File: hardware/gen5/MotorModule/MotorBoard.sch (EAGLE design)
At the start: 44 parts

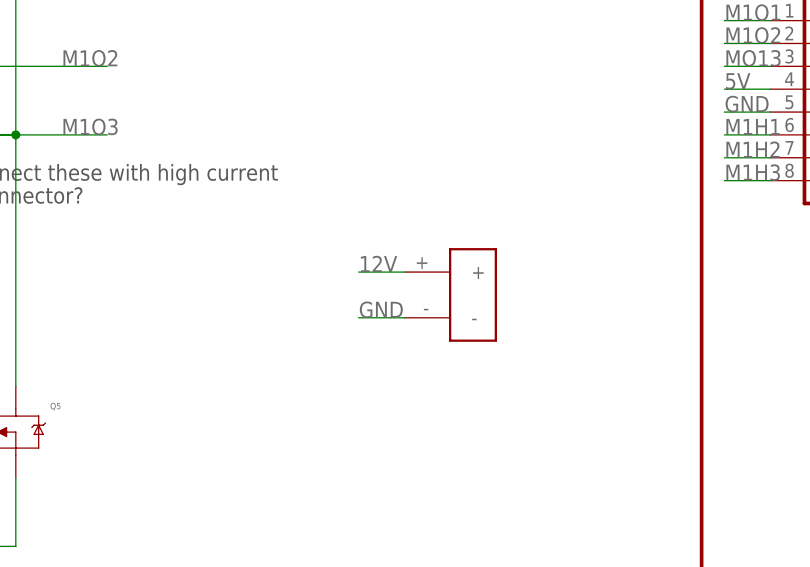
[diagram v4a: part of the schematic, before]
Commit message: placement ok - started rrouting
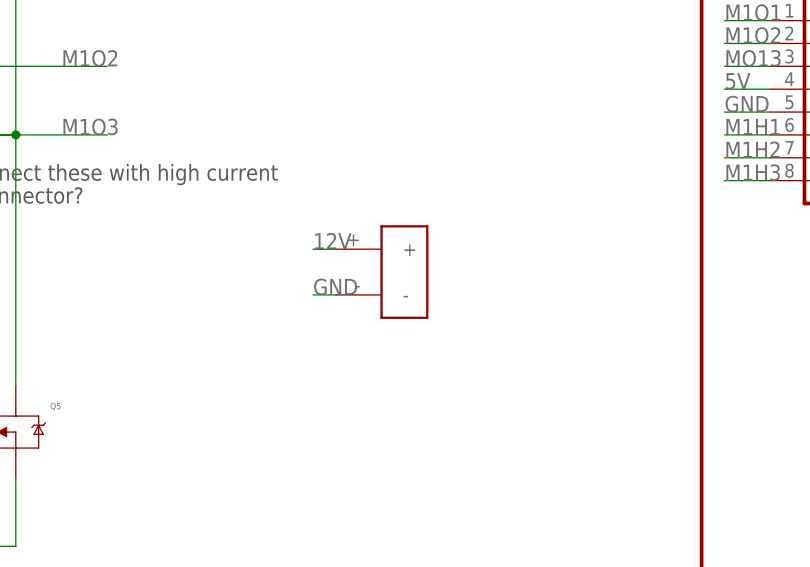
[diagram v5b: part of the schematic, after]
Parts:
- removed U$3: POWER_CONN_2X1, Kicker:POWER_CONN_2X1
- added U$2: POWER_CONN_2X1, Kicker:POWER_CONN_2X1
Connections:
- net 12V: now also U$2.+; no longer U$3.+
- net GND: now also U$2.-; no longer U$3.-
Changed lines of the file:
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@@
 <part name="J2" library="SparkFun-Connectors" library_urn="urn:adsk.eagle:library:513" deviceset="CONN_05X2" device="SHD" package3d_urn="urn:adsk.eagle:package:38000/1"/>
 <part name="J3" library="SparkFun-Connectors" library_urn="urn:adsk.eagle:library:513" deviceset="CONN_08" device="LONGPADS" package3d_urn="urn:adsk.eagle:package:38142/1"/>
-<part name="U$3" library="Kicker" deviceset="POWER_CONN_2X1" device=""/>
+<part name="U$2" library="Kicker" deviceset="POWER_CONN_2X1" device=""/>
 </parts>
 <sheets>
@@
 <instance part="J2" gate="G$1" x="266.7" y="114.3"/>
 <instance part="J3" gate="G$1" x="261.62" y="66.04" rot="R180"/>
-<instance part="U$3" gate="G$1" x="223.52" y="43.18"/>
+<instance part="U$2" gate="G$1" x="215.9" y="45.72"/>
 </instances>
 <busses>
@@
 </segment>
 <segment>
-<pinref part="U$3" gate="G$1" pin="-"/>
-<wire x1="215.9" y1="40.64" x2="210.82" y2="40.64" width="0.1524" layer="91"/>
-<label x="210.82" y="40.64" size="1.778" layer="95"/>
+<pinref part="U$2" gate="G$1" pin="-"/>
+<wire x1="208.28" y1="43.18" x2="205.74" y2="43.18" width="0.1524" layer="91"/>
+<label x="205.74" y="43.18" size="1.778" layer="95"/>
 </segment>
 </net>
@@
 </segment>
 <segment>
-<pinref part="U$3" gate="G$1" pin="+"/>
-<wire x1="215.9" y1="45.72" x2="210.82" y2="45.72" width="0.1524" layer="91"/>
-<label x="210.82" y="45.72" size="1.778" layer="95"/>
+<pinref part="U$2" gate="G$1" pin="+"/>
+<wire x1="208.28" y1="48.26" x2="205.74" y2="48.26" width="0.1524" layer="91"/>
+<label x="205.74" y="48.26" size="1.778" layer="95"/>
 </segment>
 </net>

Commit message: routed, needs cleanup
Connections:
- net BRAKE: now also J2.6; no longer J2.2
- net DIR: now also J2.4; no longer J2.9
- net ENABLE: now also J2.8
- net FAULTN: now also J2.10; no longer J2.6
- net HALLOUT: now also J2.9; no longer J2.8
- net LOCKN: now also J2.2; no longer J2.10
- net M1H1: no longer J2.3
- net M1H2: no longer J2.5
- net M1H3: no longer J2.7
- net PWM: now also J2.7; no longer J2.4
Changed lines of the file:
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@@
+</segment>
+<segment>
+<pinref part="J3" gate="G$1" pin="8"/>
+<wire x1="256.54" y1="55.88" x2="251.46" y2="55.88" width="0.1524" layer="91"/>
+<label x="251.46" y="55.88" size="1.778" layer="95"/>
+</segment>
+</net>
+<net name="M1H2" class="0">
+<segment>
+<wire x1="91.44" y1="93.98" x2="91.44" y2="116.84" width="0.1524" layer="91"/>
+<pinref part="U$1" gate="G$1" pin="HV+"/>
+<label x="91.44" y="116.84" size="1.778" layer="95" rot="R90"/>
+</segment>
+<segment>
+<pinref part="R2" gate="G$1" pin="2"/>
+<wire x1="215.9" y1="129.54" x2="215.9" y2="121.92" width="0.1524" layer="91"/>
+<label x="215.9" y="121.92" size="1.778" layer="95" rot="R90"/>
+</segment>
+<segment>
+<pinref part="J3" gate="G$1" pin="7"/>
+<wire x1="256.54" y1="58.42" x2="251.46" y2="58.42" width="0.1524" layer="91"/>
+<label x="251.46" y="58.42" size="1.778" layer="95"/>
+</segment>
+</net>
+<net name="M1H1" class="0">
+<segment>
+<wire x1="86.36" y1="93.98" x2="86.36" y2="116.84" width="0.1524" layer="91"/>
+<pinref part="U$1" gate="G$1" pin="HW+"/>
+<label x="86.36" y="116.84" size="1.778" layer="95" rot="R90"/>
+</segment>
+<segment>
+<pinref part="R3" gate="G$1" pin="2"/>
+<wire x1="208.28" y1="129.54" x2="208.28" y2="121.92" width="0.1524" layer="91"/>
+<label x="208.28" y="121.92" size="1.778" layer="95" rot="R90"/>
+</segment>
+<segment>
+<pinref part="J3" gate="G$1" pin="6"/>
+<wire x1="256.54" y1="60.96" x2="251.46" y2="60.96" width="0.1524" layer="91"/>
+<label x="251.46" y="60.96" size="1.778" layer="95"/>
+</segment>
+</net>
+<net name="PWM" class="0">
+<segment>
+<wire x1="25.4" y1="58.42" x2="63.5" y2="58.42" width="0.1524" layer="91"/>
+<label x="25.4" y="58.42" size="1.778" layer="95"/>
+<pinref part="U$1" gate="G$1" pin="PWM"/>
 </segment>
 <segment>
@@
 <label x="254" y="111.76" size="1.778" layer="95"/>
 </segment>
-<segment>
-<pinref part="J3" gate="G$1" pin="8"/>
-<wire x1="256.54" y1="55.88" x2="251.46" y2="55.88" width="0.1524" layer="91"/>
-<label x="251.46" y="55.88" size="1.778" layer="95"/>
-</segment>
-</net>
-<net name="M1H2" class="0">
-<segment>
-<wire x1="91.44" y1="93.98" x2="91.44" y2="116.84" width="0.1524" layer="91"/>
-<pinref part="U$1" gate="G$1" pin="HV+"/>
-<label x="91.44" y="116.84" size="1.778" layer="95" rot="R90"/>
-</segment>
-<segment>
-<pinref part="R2" gate="G$1" pin="2"/>
-<wire x1="215.9" y1="129.54" x2="215.9" y2="121.92" width="0.1524" layer="91"/>
-<label x="215.9" y="121.92" size="1.778" layer="95" rot="R90"/>
-</segment>
-<segment>
-<pinref part="J2" gate="G$1" pin="5"/>
-<wire x1="259.08" y1="114.3" x2="254" y2="114.3" width="0.1524" layer="91"/>
-<label x="254" y="114.3" size="1.778" layer="95"/>
-</segment>
-<segment>
-<pinref part="J3" gate="G$1" pin="7"/>
-<wire x1="256.54" y1="58.42" x2="251.46" y2="58.42" width="0.1524" layer="91"/>
-<label x="251.46" y="58.42" size="1.778" layer="95"/>
-</segment>
-</net>
-<net name="M1H1" class="0">
-<segment>
-<wire x1="86.36" y1="93.98" x2="86.36" y2="116.84" width="0.1524" layer="91"/>
-<pinref part="U$1" gate="G$1" pin="HW+"/>
-<label x="86.36" y="116.84" size="1.778" layer="95" rot="R90"/>
-</segment>
-<segment>
-<pinref part="R3" gate="G$1" pin="2"/>
-<wire x1="208.28" y1="129.54" x2="208.28" y2="121.92" width="0.1524" layer="91"/>
-<label x="208.28" y="121.92" size="1.778" layer="95" rot="R90"/>
-</segment>
-<segment>
-<pinref part="J2" gate="G$1" pin="3"/>
-<wire x1="259.08" y1="116.84" x2="254" y2="116.84" width="0.1524" layer="91"/>
-<label x="254" y="116.84" size="1.778" layer="95"/>
-</segment>
-<segment>
-<pinref part="J3" gate="G$1" pin="6"/>
-<wire x1="256.54" y1="60.96" x2="251.46" y2="60.96" width="0.1524" layer="91"/>
-<label x="251.46" y="60.96" size="1.778" layer="95"/>
-</segment>
-</net>
-<net name="PWM" class="0">
-<segment>
-<wire x1="25.4" y1="58.42" x2="63.5" y2="58.42" width="0.1524" layer="91"/>
-<label x="25.4" y="58.42" size="1.778" layer="95"/>
-<pinref part="U$1" gate="G$1" pin="PWM"/>
-</segment>
-<segment>
-<pinref part="J2" gate="G$1" pin="4"/>
-<wire x1="274.32" y1="116.84" x2="281.94" y2="116.84" width="0.1524" layer="91"/>
-<label x="279.4" y="116.84" size="1.778" layer="95"/>
-</segment>
 </net>
 <net name="BRAKE" class="0">
@@
 </segment>
 <segment>
-<pinref part="J2" gate="G$1" pin="2"/>
-<wire x1="274.32" y1="119.38" x2="279.4" y2="119.38" width="0.1524" layer="91"/>
-<label x="279.4" y="119.38" size="1.778" layer="95"/>
+<pinref part="J2" gate="G$1" pin="6"/>
+<wire x1="274.32" y1="114.3" x2="279.4" y2="114.3" width="0.1524" layer="91"/>
+<label x="276.86" y="114.3" size="1.778" layer="95"/>
 </segment>
 </net>
@@
 </segment>
 <segment>
-<pinref part="J2" gate="G$1" pin="6"/>
-<wire x1="274.32" y1="114.3" x2="279.4" y2="114.3" width="0.1524" layer="91"/>
-<label x="276.86" y="114.3" size="1.778" layer="95"/>
+<pinref part="J2" gate="G$1" pin="10"/>
+<wire x1="274.32" y1="109.22" x2="279.4" y2="109.22" width="0.1524" layer="91"/>
+<label x="276.86" y="109.22" size="1.778" layer="95"/>
 </segment>
 </net>
@@
 </segment>
 <segment>
-<pinref part="J2" gate="G$1" pin="8"/>
-<wire x1="274.32" y1="111.76" x2="279.4" y2="111.76" width="0.1524" layer="91"/>
-<label x="276.86" y="111.76" size="1.778" layer="95"/>
+<pinref part="J2" gate="G$1" pin="9"/>
+<wire x1="259.08" y1="109.22" x2="254" y2="109.22" width="0.1524" layer="91"/>
+<label x="254" y="109.22" size="1.778" layer="95"/>
 </segment>
 </net>
@@
 <label x="93.98" y="175.26" size="1.778" layer="95"/>
 </segment>
+<segment>
+<pinref part="J2" gate="G$1" pin="8"/>
+<wire x1="274.32" y1="111.76" x2="279.4" y2="111.76" width="0.1524" layer="91"/>
+<label x="276.86" y="111.76" size="1.778" layer="95"/>
+</segment>
 </net>
 <net name="DIR" class="0">
@@
 </segment>
 <segment>
-<pinref part="J2" gate="G$1" pin="9"/>
-<wire x1="259.08" y1="109.22" x2="254" y2="109.22" width="0.1524" layer="91"/>
-<label x="254" y="109.22" size="1.778" layer="95"/>
+<pinref part="J2" gate="G$1" pin="4"/>
+<wire x1="274.32" y1="116.84" x2="281.94" y2="116.84" width="0.1524" layer="91"/>
+<label x="279.4" y="116.84" size="1.778" layer="95"/>
 </segment>
 </net>
@@
 </segment>
 <segment>
-<pinref part="J2" gate="G$1" pin="10"/>
-<wire x1="274.32" y1="109.22" x2="279.4" y2="109.22" width="0.1524" layer="91"/>
-<label x="276.86" y="109.22" size="1.778" layer="95"/>
-</segment>
-</net>
+<pinref part="J2" gate="G$1" pin="2"/>
+<wire x1="274.32" y1="119.38" x2="279.4" y2="119.38" width="0.1524" layer="91"/>
+<label x="279.4" y="119.38" size="1.778" layer="95"/>
+</segment>
+</net>

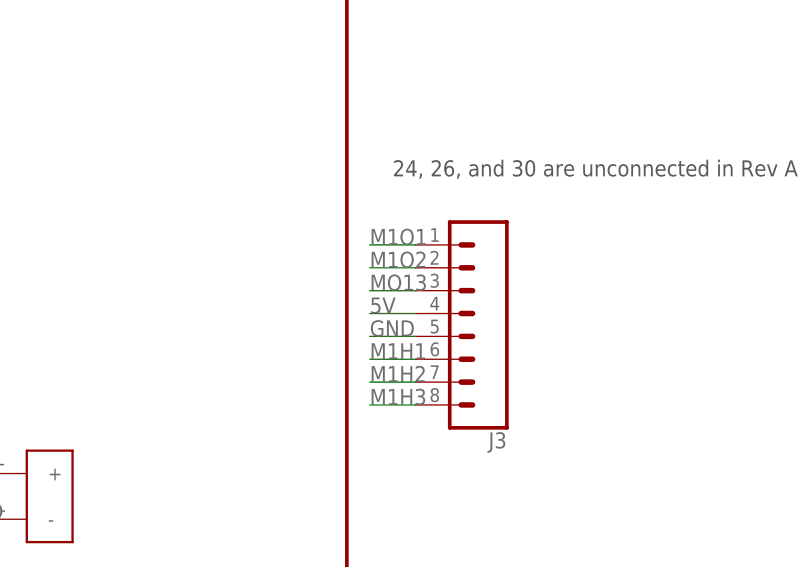
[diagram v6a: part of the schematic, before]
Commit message: redesigned motorboard 30~ traces to go
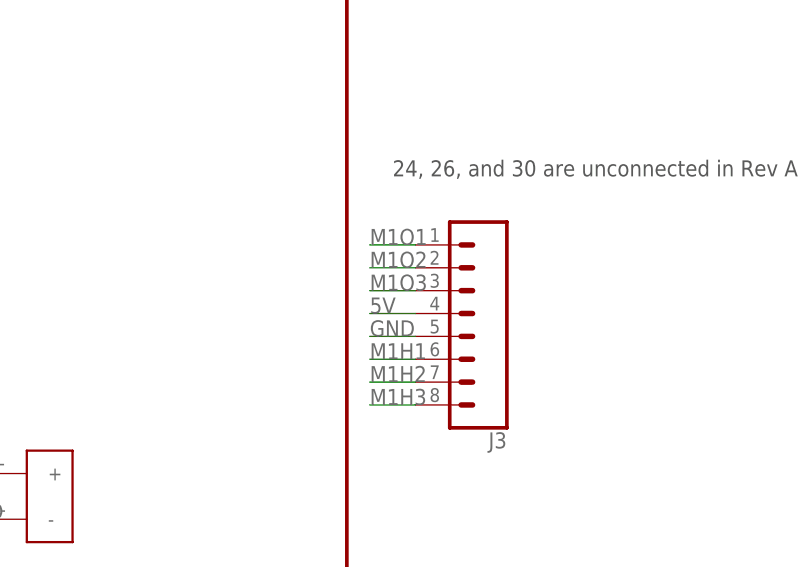
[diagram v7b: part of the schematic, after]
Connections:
- removed net MO13: J3.3
- net M1O3: now also J3.3
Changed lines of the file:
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@@
 <?xml version="1.0" encoding="utf-8"?>
 <!DOCTYPE eagle SYSTEM "eagle.dtd">
-<eagle version="8.4.0">
+<eagle version="8.3.2">
 <drawing>
 <settings>
@@
 <label x="177.8" y="60.96" size="1.778" layer="95"/>
 </segment>
+<segment>
+<pinref part="J3" gate="G$1" pin="3"/>
+<wire x1="256.54" y1="68.58" x2="251.46" y2="68.58" width="0.1524" layer="91"/>
+<label x="251.46" y="68.58" size="1.778" layer="95"/>
+</segment>
 </net>
 <net name="M1H3" class="0">
@@
 </segment>
 </net>
-<net name="MO13" class="0">
-<segment>
-<pinref part="J3" gate="G$1" pin="3"/>
-<wire x1="256.54" y1="68.58" x2="251.46" y2="68.58" width="0.1524" layer="91"/>
-<label x="251.46" y="68.58" size="1.778" layer="95"/>
-</segment>
-</net>

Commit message: nearly there
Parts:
- R9: value 0 -> 10k
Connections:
- net ENABLE: no longer R9.1
- net FAULTN: now also R9.1
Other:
- moved on the sheet: R9
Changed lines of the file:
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@@
 <part name="R5" library="SparkFun-Resistors" deviceset="RESISTOR" device="0805-RES" value="10k"/>
 <part name="R7" library="SparkFun-Resistors" deviceset="RESISTOR" device="0805-RES" value="10k"/>
-<part name="R9" library="SparkFun-Resistors" deviceset="RESISTOR" device="0805-RES" value="0"/>
+<part name="R9" library="SparkFun-Resistors" deviceset="RESISTOR" device="0805-RES" value="10k"/>
 <part name="J2" library="SparkFun-Connectors" library_urn="urn:adsk.eagle:library:513" deviceset="CONN_05X2" device="SHD" package3d_urn="urn:adsk.eagle:package:38000/1"/>
 <part name="J3" library="SparkFun-Connectors" library_urn="urn:adsk.eagle:library:513" deviceset="CONN_08" device="LONGPADS" package3d_urn="urn:adsk.eagle:package:38142/1"/>
@@
 <instance part="R5" gate="G$1" x="38.1" y="78.74" rot="R90"/>
 <instance part="R7" gate="G$1" x="45.72" y="73.66" rot="R90"/>
-<instance part="R9" gate="G$1" x="58.42" y="35.56" rot="R90"/>
+<instance part="R9" gate="G$1" x="50.8" y="68.58" rot="R90"/>
 <instance part="J2" gate="G$1" x="266.7" y="114.3"/>
 <instance part="J3" gate="G$1" x="261.62" y="66.04" rot="R180"/>
@@
 <segment>
 <pinref part="U$1" gate="G$1" pin="FAULTN"/>
-<wire x1="63.5" y1="63.5" x2="25.4" y2="63.5" width="0.1524" layer="91"/>
+<wire x1="63.5" y1="63.5" x2="50.8" y2="63.5" width="0.1524" layer="91"/>
 <label x="25.4" y="63.5" size="1.778" layer="95"/>
+<pinref part="R9" gate="G$1" pin="1"/>
+<wire x1="50.8" y1="63.5" x2="25.4" y2="63.5" width="0.1524" layer="91"/>
+<junction x="50.8" y="63.5"/>
 </segment>
 <segment>
@@
 <net name="ENABLE" class="0">
 <segment>
-<wire x1="76.2" y1="27.94" x2="58.42" y2="27.94" width="0.1524" layer="91"/>
+<wire x1="76.2" y1="27.94" x2="48.26" y2="27.94" width="0.1524" layer="91"/>
 <label x="48.26" y="27.94" size="1.778" layer="95"/>
 <pinref part="U$1" gate="G$1" pin="ENABLEN"/>
-<wire x1="58.42" y1="27.94" x2="48.26" y2="27.94" width="0.1524" layer="91"/>
 <wire x1="76.2" y1="35.56" x2="76.2" y2="27.94" width="0.1524" layer="91"/>
-<pinref part="R9" gate="G$1" pin="1"/>
-<wire x1="58.42" y1="27.94" x2="58.42" y2="30.48" width="0.1524" layer="91"/>
-<junction x="58.42" y="27.94"/>
 </segment>
 <segment>
@@
 <segment>
 <pinref part="R9" gate="G$1" pin="2"/>
-<wire x1="58.42" y1="40.64" x2="58.42" y2="43.18" width="0.1524" layer="91"/>
-<label x="58.42" y="43.18" size="1.778" layer="95"/>
-</segment>
-<segment>
+<wire x1="50.8" y1="73.66" x2="50.8" y2="76.2" width="0.1524" layer="91"/>
+<label x="50.8" y="76.2" size="1.778" layer="95"/>
+</segment>
+<segment>
